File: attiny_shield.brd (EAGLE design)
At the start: 68.6 x 53.3 mm, 13 parts, among them IC1 TINY13-20PU

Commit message: - clean-up
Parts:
- 85_V_84: device SparkFun-Switches:SWITCH_DPDT_SMD_AYZ0202 -> PianoPiano:SPARKFUN-SWITCHES_SWITCH_DPDT_SMD_AYZ0202
- moved C1 16.9 mm to (11.4, 20.2), turned to 270 degrees
- moved J8 12.7 mm to (63.5, 2.54), turned to 180 degrees
- turned PROGRAM_SWITCH to 180 degrees
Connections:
- removed net N$9: C1.1, PROGRAM_SWITCH.3
- new net N$1: C1.1, PROGRAM_SWITCH.1
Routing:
- net GND: track 64.9 -> 10.2 mm
- net N$9: track 27.4 -> 0.00 mm
- net MOSI: track 57.7 -> 69.9 mm
- net MISO: track 45.2 -> 53.5 mm
- net SCK: track 46.9 -> 53.4 mm
- net N$10: track 47.6 -> 44.4 mm
- net N$1: track 0.00 -> 2.77 mm
- net VCC_85: track 59.8 -> 61.6 mm
- added copper zone on layer 1, net GND
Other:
- board text added: "7 ~6 ~5 4 ~3 2 TX/1 RX/0"
- board text added: "A0 A1 A2 A3 A4 A5"
- board text added: "AREF GND 13 12 ~11 ~10 ~9 8"
- board text added: "RST 3V3 5V GND GND VIN"

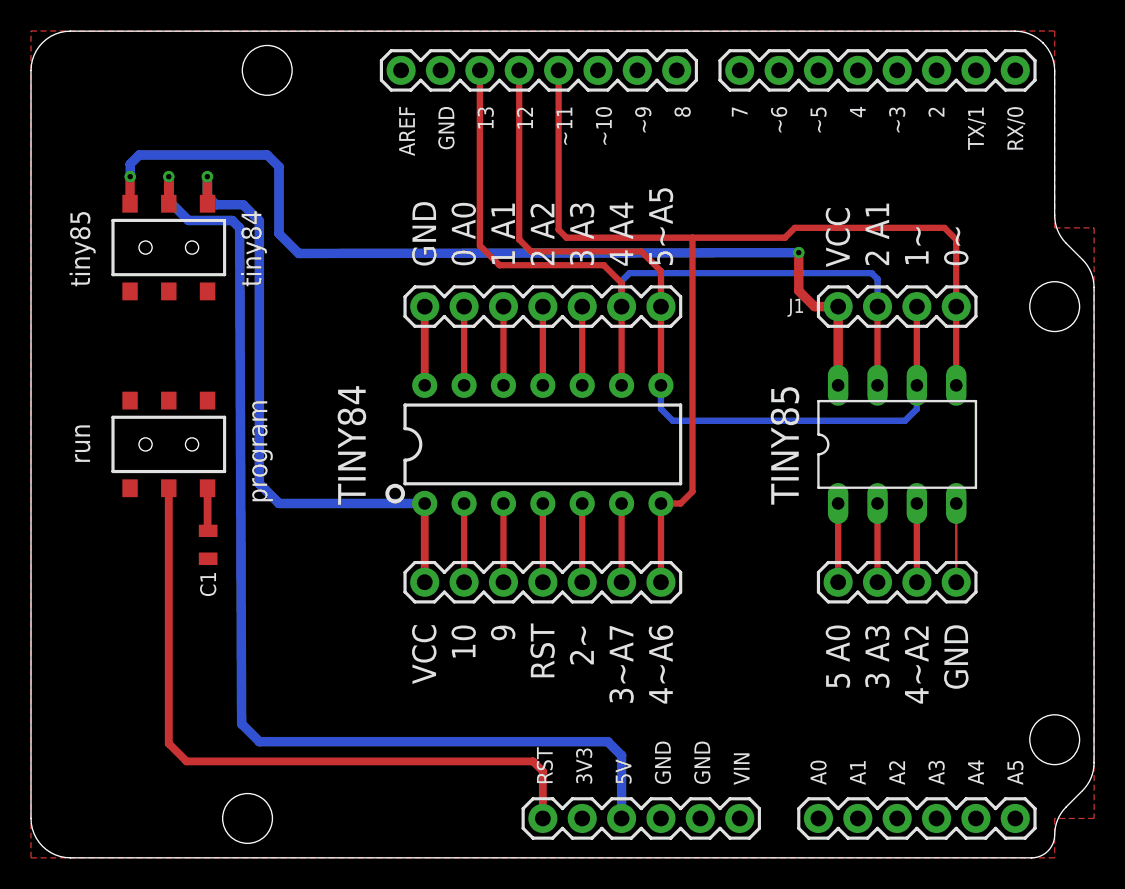
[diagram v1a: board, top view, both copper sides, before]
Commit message: added caps and pull-ups. added reset button.
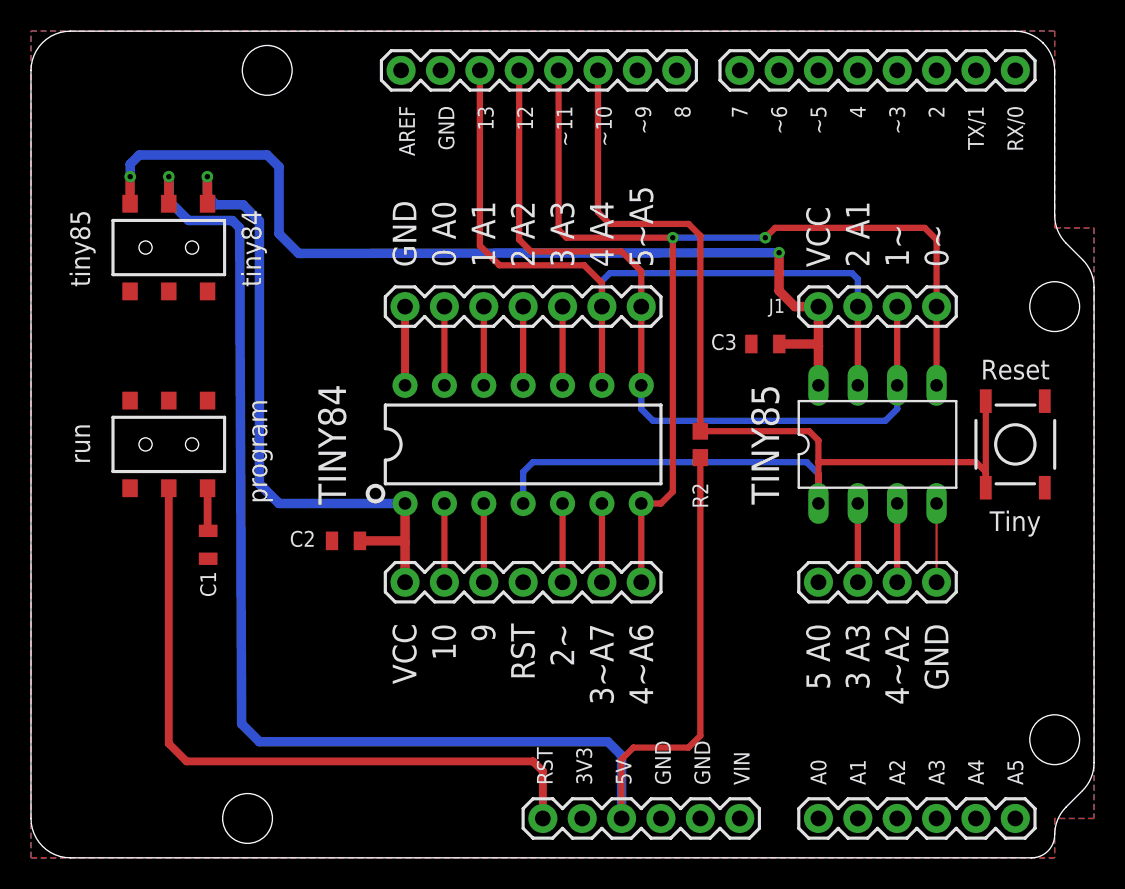
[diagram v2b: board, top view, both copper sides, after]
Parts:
- added C2, C3: 10uF, SparkFun-Capacitors:0805
- added R2: 10k, PianoPiano:SPARKFUN-RESISTORS_0603
- added S1: (no value), PianoPiano:SPARKFUN-SWITCHES_TACTILE_SWITCH_SMD_5.2MM
- moved IC1 1.27 mm to (54.6, 26.7)
- moved J1 1.27 mm to (50.8, 35.6)
- moved J4 1.27 mm to (50.8, 17.8)
- moved U$1 1.27 mm to (31.8, 26.7)
- moved J2 1.27 mm to (24.1, 35.6)
- moved J3 1.27 mm to (24.1, 17.8)
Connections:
- removed net RESET: J5.3
- new net TINY_RESET: IC1.1, J5.3, R2.1, S1.3, S1.4, U$1.4
- net 84_RESET: no longer U$1.4
- net 85_RESET: no longer IC1.1
- net GND: now also C2.2, C3.1, S1.1, S1.2
- net VCC_5V: now also R2.2
- net VCC_84: now also C2.1
- net VCC_85: now also C3.2
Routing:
- net TINY_RESET: track 0.00 -> 84.1 mm
- net VCC_5V: track 70.1 -> 97.6 mm
- net 85_RESET: track 5.08 -> 0.00 mm
- net 84_RESET: track 5.08 -> 0.00 mm
- net VCC_84: track 40.2 -> 41.9 mm
- net VCC_85: track 61.6 -> 62.9 mm
- net SCK: track 53.4 -> 52.2 mm
- net MISO: track 53.5 -> 52.3 mm
- net MOSI: track 69.9 -> 68.7 mm, vias 0 -> 2
- added copper zone on layer 16, net GND
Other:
- board text added: "Reset"
- board text added: "Tiny"
